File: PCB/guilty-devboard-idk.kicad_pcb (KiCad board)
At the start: 6 copper layers, 17.8 x 33.2 mm, 60 parts, among them J1 USB_C_Receptacle_USB2.0_16P, Q1 SP2038CNQ, U1 nRF54LM20A-QGAA, U2 SGM40567-4.2XG/TR, U3 Xiao nRF52840 Connectors, U4 TCA9536, U5 FH9261-G3JH, U6 BD83070GWL-E2, Y1 32MHz, Y2 32.768kHz

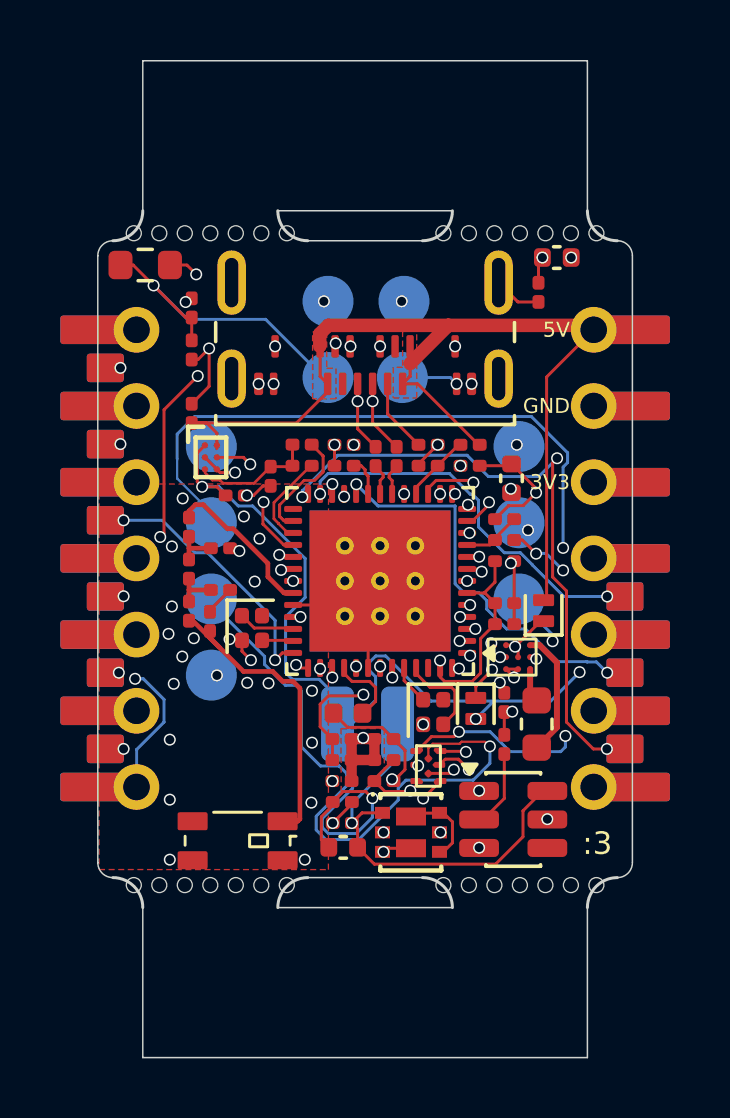
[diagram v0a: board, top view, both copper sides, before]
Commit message: remove vbus zone, fix drc errors
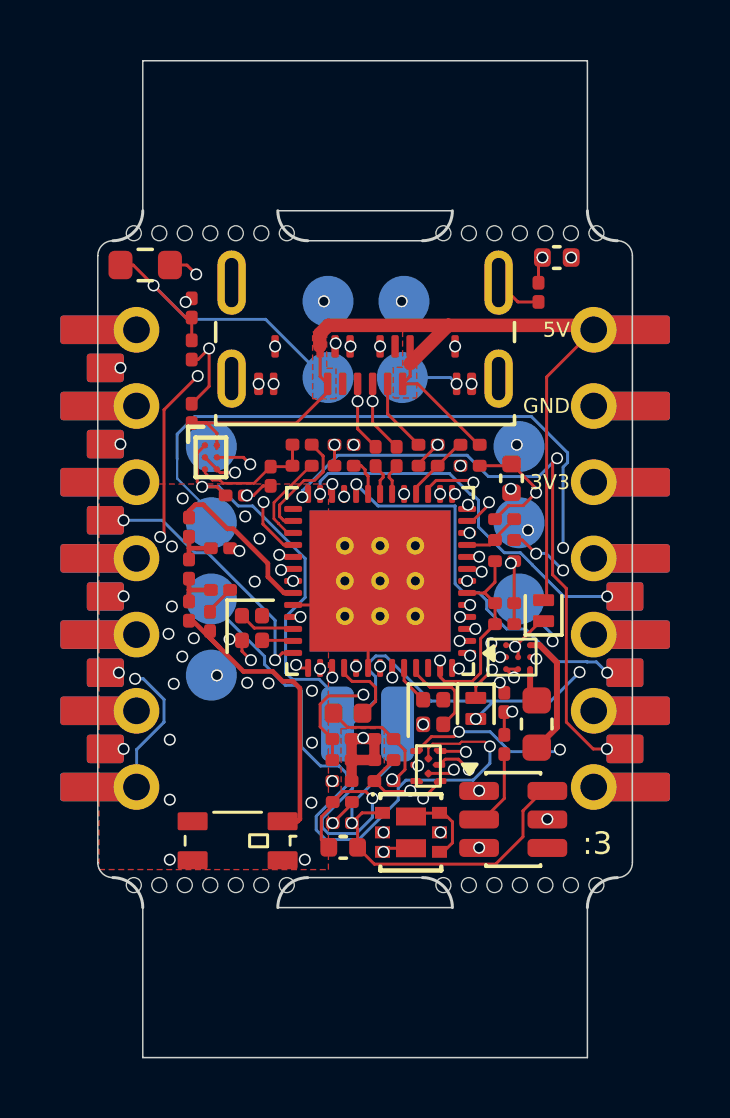
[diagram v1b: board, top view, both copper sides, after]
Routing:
- net +3V3: track 19.9 -> 17.2 mm
- removed copper zone on In2.Cu, net VBUS
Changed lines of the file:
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@@
 	)
 	(segment
-		(start 90.533 47.797)
-		(end 90.69 47.64)
+		(start 90.528 53.13867)
+		(end 91.44 54.05067)
 		(width 0.1)
 		(layer "In2.Cu")
@@
 	)
 	(segment
-		(start 89.05175 55.12825)
-		(end 88.83298 55.34702)
-		(width 0.1)
-		(layer "In2.Cu")
-		(net "+3V3")
-	)
-	(segment
-		(start 91.445 55.12825)
-		(end 91.445 53.878013)
+		(start 90.528 47.802)
+		(end 90.528 53.13867)
 		(width 0.1)
 		(layer "In2.Cu")
@@
 	)
 	(segment
-		(start 91.445 53.878013)
-		(end 90.533 52.966013)
-		(width 0.1)
-		(layer "In2.Cu")
-		(net "+3V3")
-	)
-	(segment
-		(start 90.533 52.966013)
-		(end 90.533 47.797)
+		(start 91.44 54.05067)
+		(end 91.44 55.1283)
 		(width 0.1)
 		(layer "In2.Cu")
@@
 	)
 	(segment
-		(start 91.445 55.12825)
-		(end 89.05175 55.12825)
+		(start 90.69 47.64)
+		(end 90.528 47.802)
 		(width 0.1)
 		(layer "In2.Cu")
@@
 	)
 	(via
-		(at 79.78 56.27)
+		(at 79.825703 56.269999)
 		(size 0.4)
 		(drill 0.3)
@@
 	)
 	(via
-		(at 90.497598 63.585588)
+		(at 90.315 64.04)
 		(size 0.4)
 		(drill 0.3)
@@
 	)
 	(segment
-		(start 90.497598 63.585588)
-		(end 90.497598 63.952402)
-		(width 0.1)
-		(layer "B.Cu")
-		(net "/IO_EXT_P0_D21")
-	)
-	(segment
 		(start 78.140786 52.9398)
 		(end 77.555 53.525586)
@@
 	)
 	(segment
+		(start 88.650548 64.11)
+		(end 87.987834 63.447286)
+		(width 0.1)
+		(layer "B.Cu")
+		(net "/IO_EXT_P0_D21")
+	)
+	(segment
 		(start 78.695 56.146859)
 		(end 77.555 55.006859)
@@
 	)
 	(segment
-		(start 90.497598 63.952402)
-		(end 90.34 64.11)
+		(start 90.315 64.04)
+		(end 90.245 64.11)
 		(width 0.1)
 		(layer "B.Cu")
@@
 	)
 	(segment
-		(start 88.650548 64.11)
-		(end 87.987834 63.447286)
+		(start 77.555 53.525586)
+		(end 77.555 54.354014)
 		(width 0.1)
 		(layer "B.Cu")
@@
 	)
 	(segment
-		(start 77.555 53.525586)
-		(end 77.555 54.354014)
+		(start 90.57 54.145586)
+		(end 89.364214 52.9398)
 		(width 0.1)
 		(layer "B.Cu")
@@
 	)
 	(segment
-		(start 90.34 64.11)
-		(end 88.650548 64.11)
+		(start 90.42 54.624975)
+		(end 90.57 54.474975)
 		(width 0.1)
 		(layer "B.Cu")
@@
 	)
 	(segment
-		(start 90.57 54.145586)
-		(end 89.364214 52.9398)
+		(start 90.245 64.11)
+		(end 88.650548 64.11)
 		(width 0.1)
 		(layer "B.Cu")
@@
 	)
 	(segment
-		(start 90.42 54.624975)
-		(end 90.57 54.474975)
+		(start 90.07 59.934192)
+		(end 90.07 57.66825)
 		(width 0.1)
-		(layer "B.Cu")
+		(layer "In1.Cu")
 		(net "/IO_EXT_P0_D21")
 	)
 	(segment
-		(start 90.497598 60.447597)
-		(end 90.497598 63.585588)
+		(start 90.420001 60.37)
+		(end 90.420001 60.284193)
 		(width 0.1)
 		(layer "In1.Cu")
@@
 	)
 	(segment
-		(start 90.42 57.31825)
-		(end 90.07 57.66825)
+		(start 90.07 57.66825)
+		(end 90.42 57.31825)
 		(width 0.1)
 		(layer "In1.Cu")
@@
 	)
 	(segment
-		(start 90.07 57.66825)
+		(start 90.420001 60.284193)
 		(end 90.07 59.934192)
 		(width 0.1)
@@
 	)
 	(segment
-		(start 90.420001 60.284193)
-		(end 90.420001 60.37)
+		(start 90.315 64.04)
+		(end 90.497598 63.857402)
 		(width 0.1)
 		(layer "In1.Cu")
@@
 	)
 	(segment
-		(start 90.07 59.934192)
-		(end 90.420001 60.284193)
+		(start 90.497598 63.857402)
+		(end 90.497598 60.447597)
 		(width 0.1)
 		(layer "In1.Cu")
@@
 	)
 	(segment
-		(start 90.420001 60.37)
-		(end 90.497598 60.447597)
+		(start 90.497598 60.447597)
+		(end 90.420001 60.37)
 		(width 0.1)
 		(layer "In1.Cu")
@@
 	(segment
 		(start 91.88 64.02)
-		(end 91.426987 64.02)
+		(end 91.421937 64.02)
 		(width 0.1)
 		(layer "F.Cu")
@@
 	)
 	(segment
-		(start 91.426987 64.02)
-		(end 90.533 63.126013)
+		(start 90.07 58.212487)
+		(end 90.07 54.48)
 		(width 0.1)
 		(layer "F.Cu")
@@
 	)
 	(segment
-		(start 90.07 58.29)
-		(end 90.533 58.753)
+		(start 90.528 63.126063)
+		(end 90.528 58.670487)
 		(width 0.1)
 		(layer "F.Cu")
@@
 	)
 	(segment
-		(start 90.533 63.126013)
-		(end 90.533 58.753)
+		(start 90.528 58.670487)
+		(end 90.07 58.212487)
 		(width 0.1)
 		(layer "F.Cu")
@@
 	)
 	(segment
-		(start 90.07 58.29)
-		(end 90.07 54.48)
+		(start 91.421937 64.02)
+		(end 90.528 63.126063)
 		(width 0.1)
 		(layer "F.Cu")
@@
 		(polygon
 			(pts
-				(xy 84.76 52.32) (xy 85.54 52.32) (xy 85.54 50.09) (xy 85.07 50.09) (xy 85.07 51.3) (xy 84.76 51.3)
+				(xy 84.76 52.32) (xy 85.54 52.32) (xy 85.54 51.205) (xy 86.66 50.09) (xy 85.07 50.09) (xy 85.07 51.3)
+				(xy 84.76 51.3)
 			)
 		)
@@
 			)
 		)
-	)
-	(zone
-		(net "VBUS")
-		(layer "In2.Cu")
-		(hatch edge 0.5)
-		(priority 1)
-		(connect_pads
-			(clearance 0.15)
-		)
-		(min_thickness 0.25)
-		(fill yes
-			(thermal_gap 0.5)
-			(thermal_bridge_width 0.5)
-			(island_removal_mode 0)
-		)
-		(polygon
-			(pts
-				(xy 89.75 54.2) (xy 89.75 47.13) (xy 78.87 47.12) (xy 78.87 54.2)
-			)
-		)

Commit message: increase corner rounding
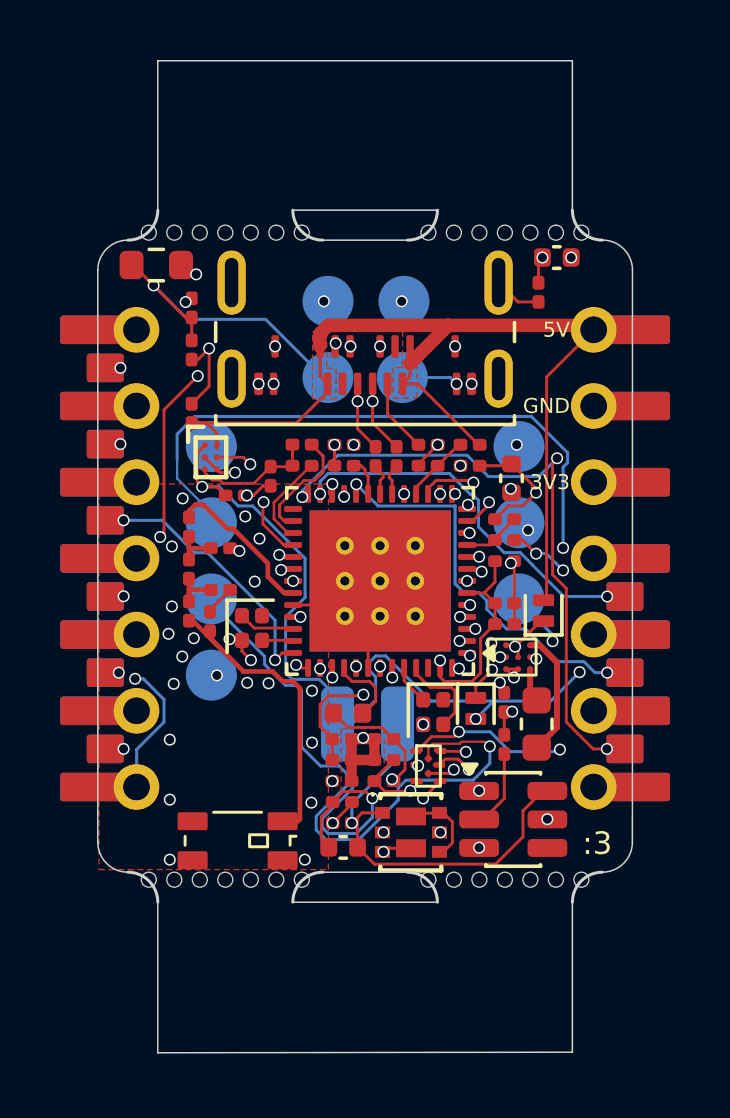
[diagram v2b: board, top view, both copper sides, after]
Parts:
- moved REF** 0.53 mm to (88.5, 68.1)
- moved REF** 0.53 mm to (79.2, 68.1)
- moved REF** 0.50 mm to (88.5, 47.1)
- moved REF** 0.50 mm to (79.2, 47.1)
- moved JP1 0.37 mm to (76.9, 47.9)
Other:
- board size 17.8 x 33.2 mm -> 17.8 x 33.1 mm
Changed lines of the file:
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@@
 	(footprint "Panelization:MouseBite-Part_2.0x4.5mm_outset_D0.5mm_P0.85mm_7h"
 		(layer "F.Cu")
-		(at 88.98 68.308 180)
+		(at 88.48 68.128 180)
 		(descr "Break slot 2mm part, standard: L=4.5mm, holes outset (sand flat with edge)")
 		(tags "mousebite stamp slot break tab 2mm edge outset")
@@
 	(footprint "Panelization:MouseBite-Part_2.0x4.5mm_outset_D0.5mm_P0.85mm_7h"
 		(layer "F.Cu")
-		(at 88.98 47.08)
+		(at 88.48 47.06)
 		(descr "Break slot 2mm part, standard: L=4.5mm, holes outset (sand flat with edge)")
 		(tags "mousebite stamp slot break tab 2mm edge outset")
@@
 	(footprint "Panelization:MouseBite-Part_2.0x4.5mm_outset_D0.5mm_P0.85mm_7h"
 		(layer "F.Cu")
-		(at 78.66 47.08)
+		(at 79.16 47.06)
 		(descr "Break slot 2mm part, standard: L=4.5mm, holes outset (sand flat with edge)")
 		(tags "mousebite stamp slot break tab 2mm edge outset")
@@
 	(footprint "Resistor_SMD:R_0603_1608Metric"
 		(layer "F.Cu")
-		(at 76.49 47.89)
+		(at 76.86 47.89)
 		(descr "Resistor SMD 0603 (1608 Metric), square (rectangular) end terminal, IPC-7351 nominal, (Body size source: IPC-SM-782 page 72, https://www.pcb-3d.com/wordpress/wp-content/uploads/ipc-sm-782a_amendment_1_and_2.pdf)")
 		(tags "resistor")
@@
 	(footprint "Panelization:MouseBite-Part_2.0x4.5mm_outset_D0.5mm_P0.85mm_7h"
 		(layer "F.Cu")
-		(at 78.66 68.308 180)
+		(at 79.16 68.128 180)
 		(descr "Break slot 2mm part, standard: L=4.5mm, holes outset (sand flat with edge)")
 		(tags "mousebite stamp slot break tab 2mm edge outset")
@@
 		)
 		(property "Value" "FH9261-G3JH"
-			(at 0 2.4 0)
+			(at 0 2.24 0)
 			(layer "F.Fab")
 			(effects
@@
 	)
 	(gr_arc
-		(start 74.91 47.58)
-		(mid 75.056447 47.226447)
-		(end 75.41 47.08)
+		(start 74.91 48.06)
+		(mid 75.202893 47.352893)
+		(end 75.91 47.06)
 		(stroke
 			(width 0.05)
@@
 	)
 	(gr_line
-		(start 74.91 67.808)
-		(end 74.91 47.58)
+		(start 74.91 67.128)
+		(end 74.91 48.06)
 		(stroke
 			(width 0.05)
@@
 	)
 	(gr_arc
-		(start 75.41 68.308)
-		(mid 75.056447 68.161553)
-		(end 74.91 67.808)
+		(start 75.91 68.128)
+		(mid 75.202893 67.835107)
+		(end 74.91 67.128)
 		(stroke
 			(width 0.05)
@@
 	)
 	(gr_line
-		(start 76.41 41.08)
-		(end 76.41 46.08)
+		(start 76.91 41.08)
+		(end 76.91 46.057499)
 		(stroke
 			(width 0.05)
@@
 	)
 	(gr_line
-		(start 76.41 69.308)
-		(end 76.41 74.308)
+		(start 76.91 69.128)
+		(end 76.91 74.148)
 		(stroke
 			(width 0.05)
@@
 	)
 	(gr_line
-		(start 76.41 74.308)
-		(end 91.23 74.308)
+		(start 76.91 74.148)
+		(end 90.73 74.128)
 		(stroke
 			(width 0.05)
@@
 	)
 	(gr_line
-		(start 80.91 69.308)
-		(end 86.73 69.308)
+		(start 81.41 69.128)
+		(end 86.23 69.128)
 		(stroke
 			(width 0.05)
@@
 	)
 	(gr_line
-		(start 81.91 68.308)
-		(end 85.73 68.308)
+		(start 82.41 68.128)
+		(end 85.23 68.128)
 		(stroke
 			(width 0.05)
@@
 	)
 	(gr_line
-		(start 85.73 47.08)
-		(end 81.91 47.08)
+		(start 85.23 47.06)
+		(end 82.41 47.06)
 		(stroke
 			(width 0.05)
@@
 	)
 	(gr_line
-		(start 86.73 46.08)
-		(end 80.91 46.08)
+		(start 86.23 46.06)
+		(end 81.41 46.06)
 		(stroke
 			(width 0.05)
@@
 	)
 	(gr_line
-		(start 91.23 41.08)
-		(end 76.41 41.08)
+		(start 90.73 41.08)
+		(end 76.91 41.08)
 		(stroke
 			(width 0.05)
@@
 	)
 	(gr_line
-		(start 91.23 46.08)
-		(end 91.23 41.08)
+		(start 90.73 46.06)
+		(end 90.73 41.08)
 		(stroke
 			(width 0.05)
@@
 	)
 	(gr_line
-		(start 91.23 74.308)
-		(end 91.23 69.308)
+		(start 90.73 74.128)
+		(end 90.73 69.128)
 		(stroke
 			(width 0.05)
@@
 	)
 	(gr_arc
-		(start 92.23 47.08)
-		(mid 92.583553 47.226447)
-		(end 92.73 47.58)
+		(start 91.732893 47.057107)
+		(mid 92.44 47.35)
+		(end 92.732893 48.057107)
 		(stroke
 			(width 0.05)
@@
 		(layer "Edge.Cuts")
 	)
-	(gr_line
-		(start 92.73 47.58)
-		(end 92.73 67.808)
+	(gr_arc
+		(start 92.73 67.13)
+		(mid 92.436401 67.835815)
+		(end 91.73 68.128002)
 		(stroke
 			(width 0.05)
@@
 		(layer "Edge.Cuts")
 	)
-	(gr_arc
-		(start 92.73 67.808)
-		(mid 92.583553 68.161553)
-		(end 92.23 68.308)
+	(gr_line
+		(start 92.732893 48.057107)
+		(end 92.73 67.13)
 		(stroke
 			(width 0.05)
@@
 	)
 	(barcode
-		(at 86.67 78.35 0)
-		(layer "F.SilkS")
-		(size 4 4)
-		(text "askiiart.net/xr")
-		(text_height 0.001)
-		(type microqr)
-		(ecc_level L)
-		(hide no)
-		(knockout no)
-	)
-	(barcode
 		(at 83.71 57.785 0)
 		(layer "B.SilkS")
@@
 	)
 	(segment
-		(start 77.315 47.89)
-		(end 77.88 47.89)
-		(width 0.1)
-		(layer "F.Cu")
-		(net "GND")
-	)
-	(segment
 		(start 88.709999 62.79)
 		(end 88.724999 62.775)
@@
 	)
 	(segment
-		(start 77.88 47.89)
-		(end 78.19 48.2)
+		(start 83.92 61.32)
+		(end 83.92 60.48)
 		(width 0.1)
 		(layer "F.Cu")
@@
 	)
 	(segment
-		(start 83.92 61.32)
-		(end 83.92 60.48)
+		(start 77.88 47.89)
+		(end 78.19 48.2)
 		(width 0.1)
 		(layer "F.Cu")
@@
 	)
 	(segment
+		(start 77.685 47.89)
+		(end 77.88 47.89)
+		(width 0.1)
+		(layer "F.Cu")
+		(net "GND")
+	)
+	(segment
 		(start 84.48 65.44)
 		(end 85.297526 65.44)
@@
 	)
 	(segment
-		(start 77.840001 49.64)
+		(start 76.090001 47.89)
 		(end 76.770001 48.57)
 		(width 0.1)
@@
 	)
 	(segment
-		(start 76.090001 47.89)
-		(end 75.665 47.89)
+		(start 77.840001 49.64)
+		(end 76.770001 48.57)
 		(width 0.1)
 		(layer "F.Cu")
@@
 	)
 	(segment
-		(start 76.770001 48.57)
+		(start 76.035 47.89)
 		(end 76.090001 47.89)
 		(width 0.1)
@@
 	)
 	(segment
-		(start 91.532 61.12025)
-		(end 91.22 61.12025)
-		(width 0.1)
-		(layer "B.Cu")
-		(net "/P1.07_GRTC.CLKOUTFAST")
-	)
-	(segment
 		(start 86.82 55.92)
 		(end 84.250505 55.92)
@@
 	)
 	(segment
+		(start 91.89 61.47825)
+		(end 91.483225 61.47825)
+		(width 0.1)
+		(layer "B.Cu")
+		(net "/P1.07_GRTC.CLKOUTFAST")
+	)
+	(segment
 		(start 87.115025 58.81)
 		(end 86.82 58.514975)
@@
 	)
 	(segment
-		(start 91.20975 61.11)
+		(start 91.114975 61.11)
 		(end 90.255858 61.11)
 		(width 0.1)
@@
 	)
 	(segment
-		(start 88.535786 60.0198)
-		(end 87.875 59.359014)
+		(start 91.483225 61.47825)
+		(end 91.114975 61.11)
 		(width 0.1)
 		(layer "B.Cu")
@@
 	)
 	(segment
-		(start 91.89 61.47825)
-		(end 91.532 61.12025)
+		(start 88.535786 60.0198)
+		(end 87.875 59.359014)
 		(width 0.1)
 		(layer "B.Cu")
@@
 		(width 0.1)
 		(layer "B.Cu")
-		(net "/P1.07_GRTC.CLKOUTFAST")
-	)
-	(segment
-		(start 91.22 61.12025)
-		(end 91.20975 61.11)
-		(width 0.1)
-		(layer "B.Cu")
